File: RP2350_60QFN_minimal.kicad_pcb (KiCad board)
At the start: 2 copper layers, 52 x 51 mm, 43 parts, among them J1 USB_B_Micro, J2 Conn_02x18_Odd_Even, J3 Conn_02x18_Odd_Even, J4 SM03B-SRSS-TB, SW1 SW_Push, SW2 SW_Push, U1 RP2350_60QFN, U2 NCP1117-3.3_SOT223, U3 W25Q128JVS, Y1 ABM8-272-T3

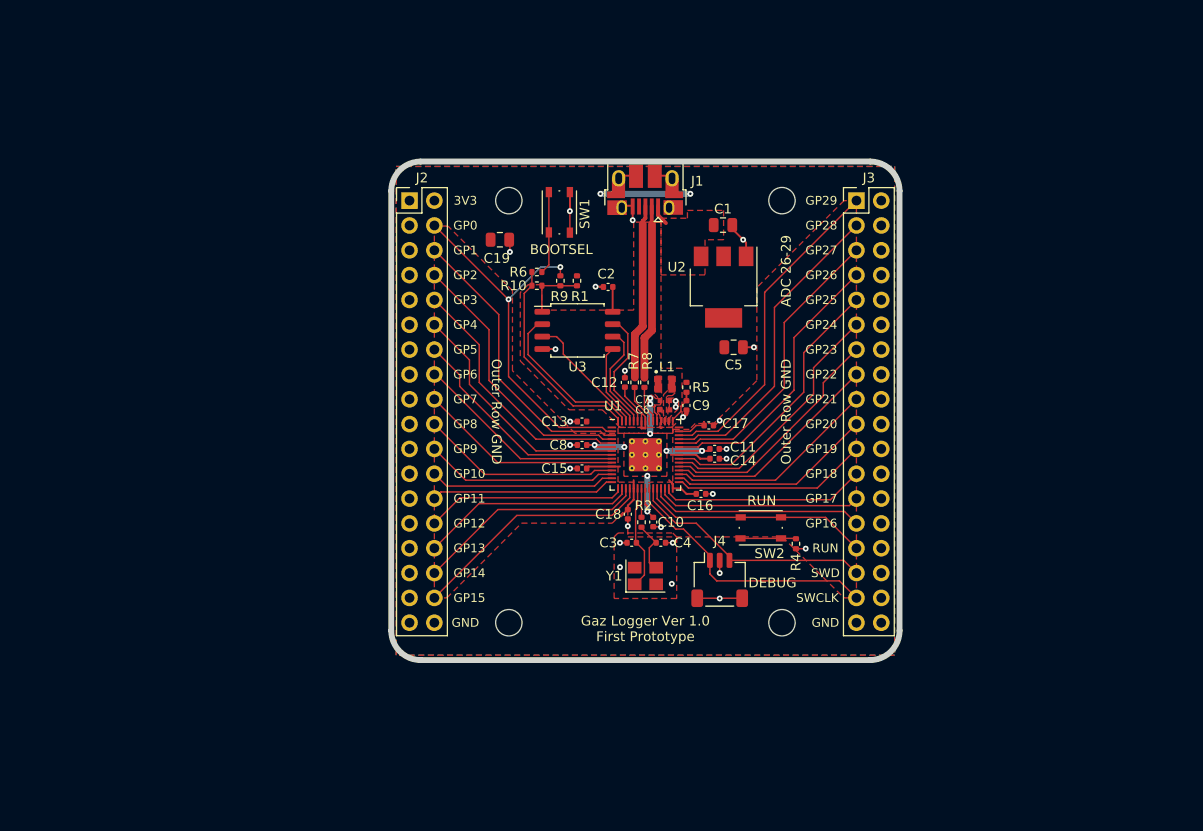
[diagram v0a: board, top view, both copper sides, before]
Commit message: improve design
Improve design, added multiplexer
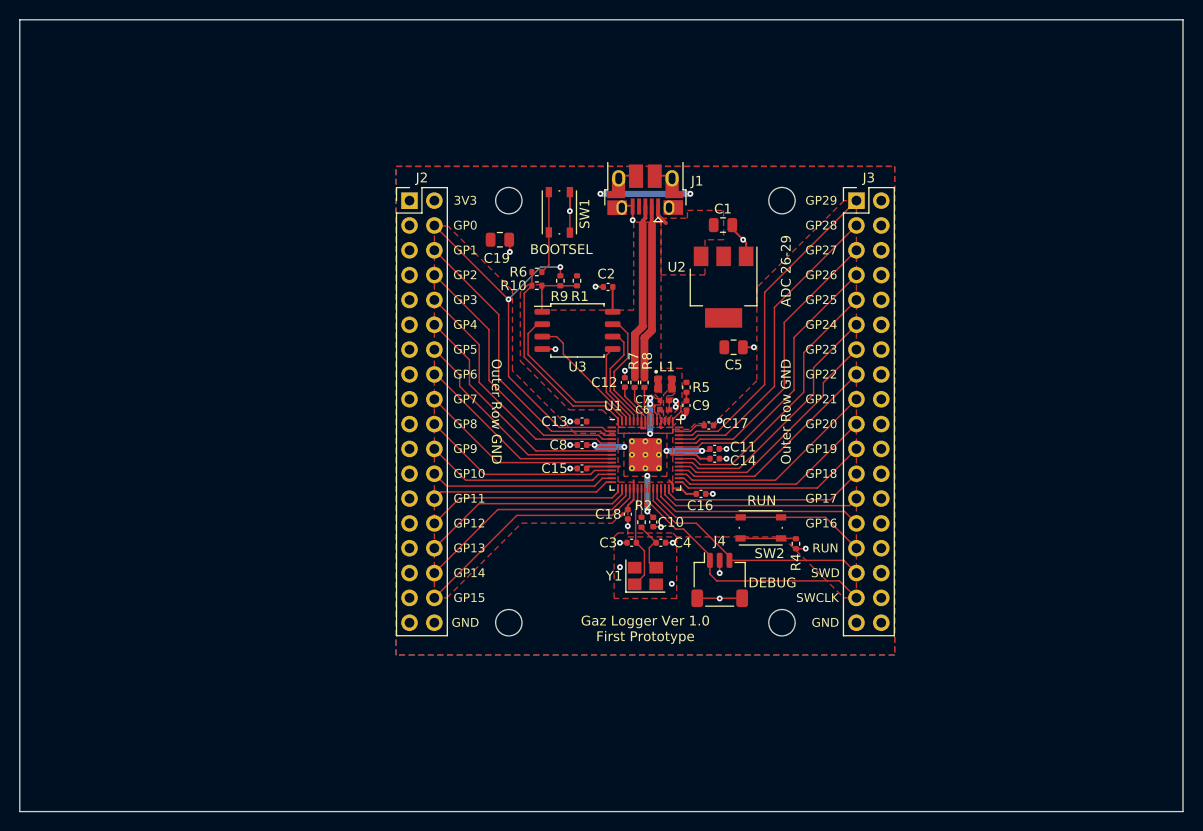
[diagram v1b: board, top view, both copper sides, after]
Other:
- board size 52 x 51 mm -> 119 x 81 mm
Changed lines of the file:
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@@
 		)
 	)
-	(gr_line
-		(start 123 121)
-		(end 77 121)
+	(gr_rect
+		(start 36 55.5)
+		(end 155 136.5)
 		(stroke
-			(width 0.6)
-			(type solid)
+			(width 0.05)
+			(type default)
 		)
+		(fill none)
 		(layer "Edge.Cuts")
 	)
-	(gr_line
-		(start 126 73)
-		(end 126 118)
-		(stroke
-			(width 0.6)
-			(type solid)
-		)
-		(layer "Edge.Cuts")
-	)
-	(gr_line
-		(start 77 70)
-		(end 123 70)
-		(stroke
-			(width 0.6)
-			(type solid)
-		)
-		(layer "Edge.Cuts")
-	)
-	(gr_line
-		(start 74 118)
-		(end 74 73)
-		(stroke
-			(width 0.6)
-			(type solid)
-		)
-		(layer "Edge.Cuts")
-	)
-	(gr_arc
-		(start 123 70)
-		(mid 125.12132 70.87868)
-		(end 126 73)
-		(stroke
-			(width 0.6)
-			(type solid)
-		)
-		(layer "Edge.Cuts")
-	)
-	(gr_arc
-		(start 74 73)
-		(mid 74.87868 70.87868)
-		(end 77 70)
-		(stroke
-			(width 0.6)
-			(type solid)
-		)
-		(layer "Edge.Cuts")
-	)
-	(gr_arc
-		(start 77 121)
-		(mid 74.87868 120.12132)
-		(end 74 118)
-		(stroke
-			(width 0.6)
-			(type solid)
-		)
-		(layer "Edge.Cuts")
-	)
-	(gr_arc
-		(start 126 118)
-		(mid 125.12132 120.12132)
-		(end 123 121)
-		(stroke
-			(width 0.6)
-			(type solid)
-		)
-		(layer "Edge.Cuts")
-	)

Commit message: added resistors matrics
added resistors matrics
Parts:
- removed C3, C4: 15p, Capacitor_SMD:C_0402_1005Metric
- removed R2: 1k, Resistor_SMD:R_0402_1005Metric
- removed Y1: ABM8-272-T3, Crystal:Crystal_SMD_3225-4Pin_3.2x2.5mm
- added C20: 15p, Capacitor_SMD:C_0402_1005Metric, F.Cu at (98.5, 109.0)
- added C21: 100nF, Capacitor_SMD:C_0402_1005Metric, F.Cu at (70.0, 76.0)
- added C22: 15p, Capacitor_SMD:C_0402_1005Metric, F.Cu at (101.5, 109.0)
- added C25: 1nF, Capacitor_SMD:C_0402_1005Metric, F.Cu at (64.0, 72.5)
- added C26: 100nF, Capacitor_SMD:C_0402_1005Metric, F.Cu at (100.5, 154.5)
- added GDT1: ~, Spark-2031-42T-SM-RPLF:TVS_2031-42T-SM-RPLF, F.Cu at (22.0, 170.0)
- added R(ACH)1: 1M, Resistor_SMD:R_0805_2012Metric_Pad1.20x1.40mm_HandSolder, F.Cu at (49.5, 67.5)
- added R11: 620k, Resistor_SMD:R_0805_2012Metric_Pad1.20x1.40mm_HandSolder, F.Cu at (23.5, 87.0)
- added R12: 390k, Resistor_SMD:R_0805_2012Metric_Pad1.20x1.40mm_HandSolder, F.Cu at (23.5, 89.5)
- added R13: 240k, Resistor_SMD:R_0805_2012Metric_Pad1.20x1.40mm_HandSolder, F.Cu at (23.5, 92.0)
- added R14: 160k, Resistor_SMD:R_0805_2012Metric_Pad1.20x1.40mm_HandSolder, F.Cu at (23.5, 94.5)
- added R15: 100k, Resistor_SMD:R_0805_2012Metric_Pad1.20x1.40mm_HandSolder, F.Cu at (23.5, 97.0)
- added R16: 62k, Resistor_SMD:R_0805_2012Metric_Pad1.20x1.40mm_HandSolder, F.Cu at (23.5, 99.5)
- added R17: 39k, Resistor_SMD:R_0805_2012Metric_Pad1.20x1.40mm_HandSolder, F.Cu at (23.5, 102.0)
- added R18: 24k, Resistor_SMD:R_0805_2012Metric_Pad1.20x1.40mm_HandSolder, F.Cu at (23.5, 104.5)
- added R19: 16k, Resistor_SMD:R_0805_2012Metric_Pad1.20x1.40mm_HandSolder, F.Cu at (23.5, 107.0)
- added R20: 10k, Resistor_SMD:R_0805_2012Metric_Pad1.20x1.40mm_HandSolder, F.Cu at (23.5, 109.5)
- added R21: 6.2k, Resistor_SMD:R_0805_2012Metric_Pad1.20x1.40mm_HandSolder, F.Cu at (23.5, 112.0)
- added R22: 3.9k, Resistor_SMD:R_0805_2012Metric_Pad1.20x1.40mm_HandSolder, F.Cu at (23.5, 114.5)
- added R23: 2.4k, Resistor_SMD:R_0805_2012Metric_Pad1.20x1.40mm_HandSolder, F.Cu at (23.5, 117.0)
- added R24: 1.6k, Resistor_SMD:R_0805_2012Metric_Pad1.20x1.40mm_HandSolder, F.Cu at (23.5, 119.5)
- added R25: 1k, Resistor_SMD:R_0805_2012Metric_Pad1.20x1.40mm_HandSolder, F.Cu at (23.5, 122.0)
- added R26: 1k, Resistor_SMD:R_0402_1005Metric, F.Cu at (99.5, 107.0)
- added R27: 10k, Resistor_SMD:R_0805_2012Metric_Pad1.20x1.40mm_HandSolder, F.Cu at (32.8, 69.5)
- added R28: 10k, Resistor_SMD:R_0805_2012Metric_Pad1.20x1.40mm_HandSolder, F.Cu at (32.8, 72.4)
- added R29: 10k, Resistor_SMD:R_0805_2012Metric_Pad1.20x1.40mm_HandSolder, F.Cu at (32.8, 75.3)
- added R3: 1M, Resistor_SMD:R_0805_2012Metric_Pad1.20x1.40mm_HandSolder, F.Cu at (23.5, 84.5)
- added U4: CD74HC4067SM96G4, CD74HC4067SM96G4:SOP65P780X200-24N, F.Cu at (64.0, 77.5)
- added U5: TLV9002IDGKR, TLV9002IDGKR:SOP65P490X110-8N, F.Cu at (23.0, 146.0)
- added U6: ADS1115IDGSR, ADS1115IDGSR:SOP50P490X110-10N, F.Cu at (41.5, 143.5)
- added U7: PCA9306DP1_125, PCA9306DP1_125:SOP65P400X110-8N, F.Cu at (53.0, 147.0)
- added Y2: ABM8-272-T3, Crystal:Crystal_SMD_3225-4Pin_3.2x2.5mm, F.Cu at (100.1, 112.3)
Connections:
- J2 pad 1: GND -> VBUS
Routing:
- net VBUS: track 2.11 -> 47.2 mm
- net GND: track 37.5 -> 68.6 mm, vias 27 -> 29
- net /GPIO0: track 39.0 -> 59.2 mm, vias 2 -> 4
- net /GPIO1: track 29.8 -> 49.2 mm, vias 0 -> 2
- net /GPIO3: track 26.5 -> 38.7 mm
- net /GPIO2: track 28.2 -> 39.6 mm
- net Net-(C4-Pad1): track 5.42 -> 0.00 mm
- net Net-(C22-Pad1): track 0.00 -> 5.42 mm
- net Net-(U4-COMMON_I/O): track 0.00 -> 3.64 mm
- net +3V3: track 37.6 -> 41.2 mm

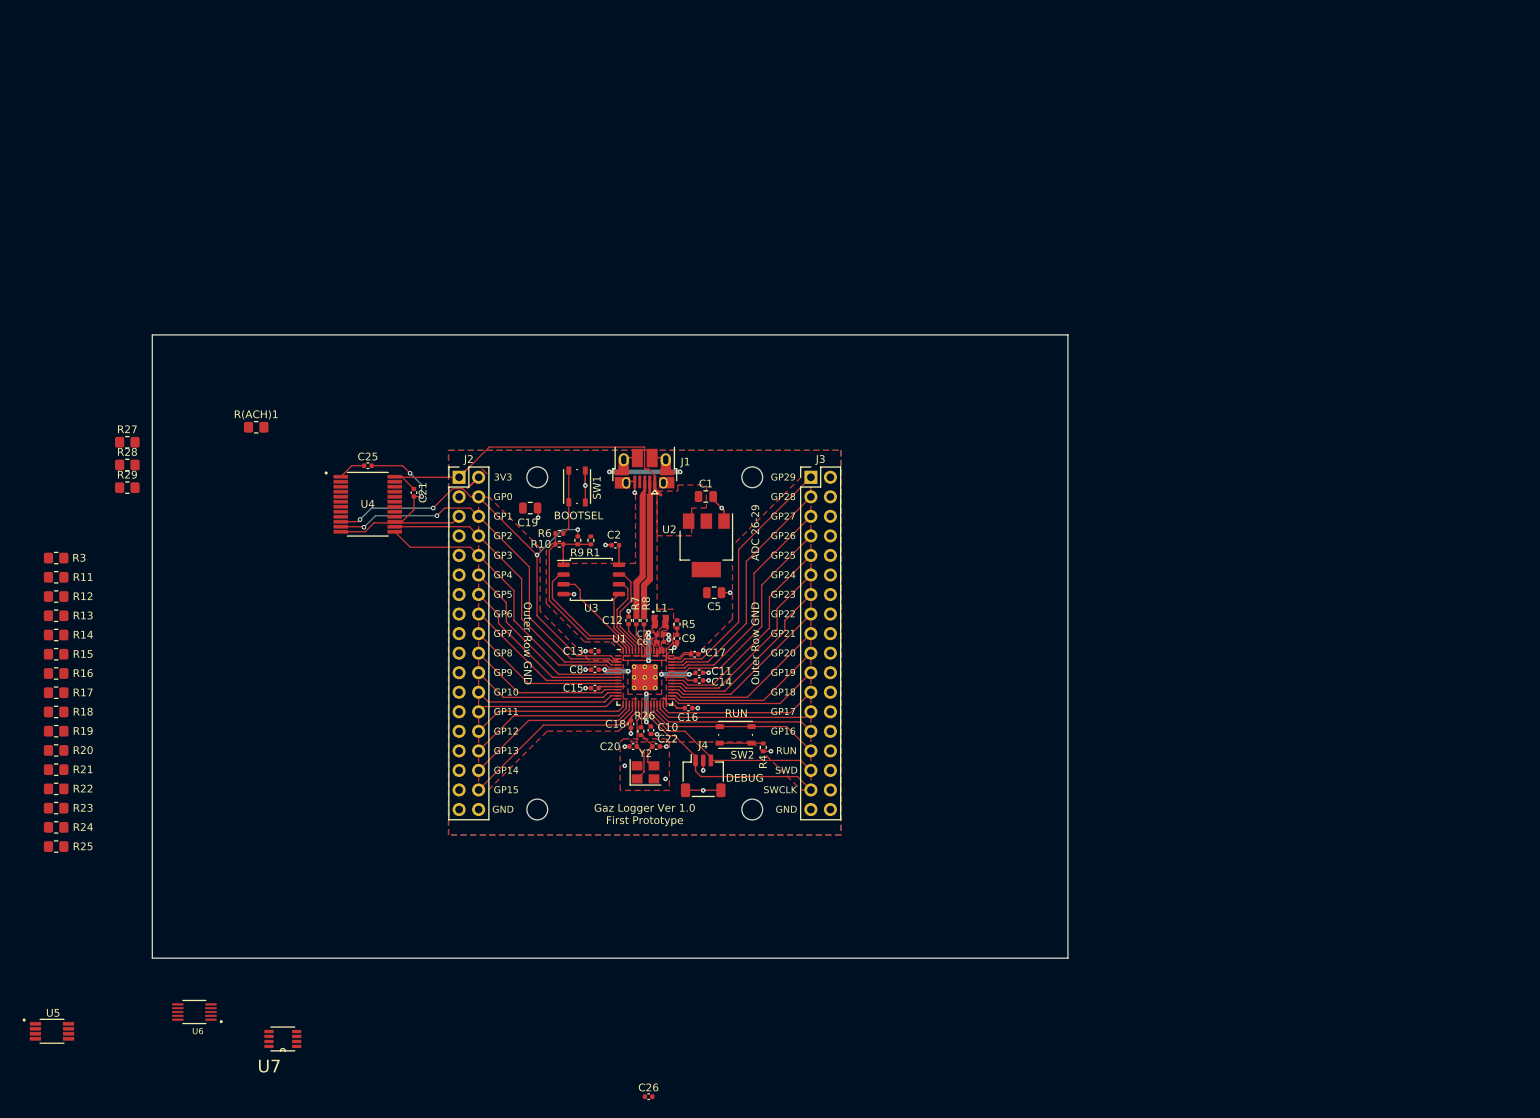
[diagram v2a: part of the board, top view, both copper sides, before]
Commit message: updare resistor matrix
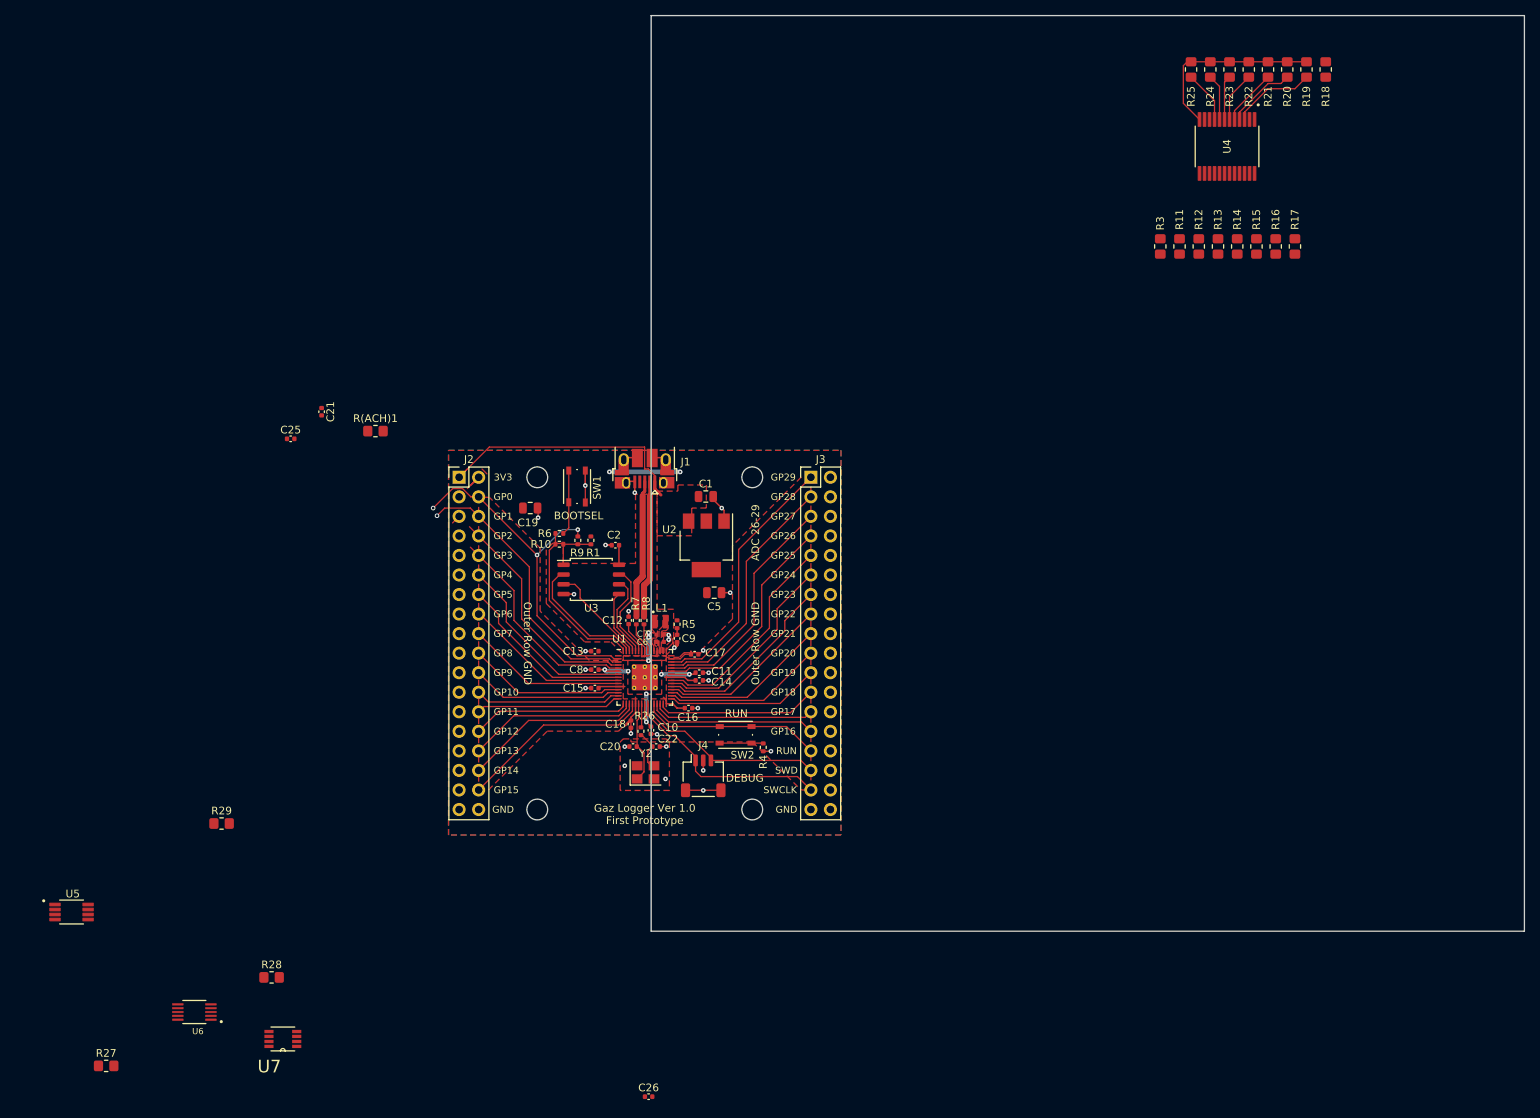
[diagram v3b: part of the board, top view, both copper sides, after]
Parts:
- moved R18 184.9 mm to (188.5, 21.0), turned to 90 degrees
- moved R19 183.9 mm to (186.0, 21.0), turned to 90 degrees
- moved R20 182.8 mm to (183.5, 21.0), turned to 90 degrees
- moved R21 181.9 mm to (181.0, 21.0), turned to 90 degrees
- moved R22 181.0 mm to (178.5, 21.0), turned to 90 degrees
- moved R23 180.2 mm to (176.0, 21.0), turned to 90 degrees
- moved R24 179.4 mm to (173.5, 21.0), turned to 90 degrees
- moved R25 178.8 mm to (171.0, 21.0), turned to 90 degrees
- moved R17 171.1 mm to (184.5, 44.0), turned to -90 degrees
- moved R16 167.9 mm to (182.0, 44.0), turned to -90 degrees
- moved R15 164.8 mm to (179.5, 44.0), turned to -90 degrees
- moved R14 161.6 mm to (177.0, 44.0), turned to -90 degrees
- moved R13 158.4 mm to (174.5, 44.0), turned to -90 degrees
- moved R12 155.3 mm to (172.0, 44.0), turned to -90 degrees
- moved R11 152.2 mm to (169.5, 44.0), turned to -90 degrees
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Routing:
- net /GPIO1: track 49.2 -> 36.1 mm, vias 2 -> 1
- net /GPIO0: track 59.2 -> 46.4 mm, vias 4 -> 3
- net VBUS: track 47.2 -> 35.6 mm
- net Net-(U4-I6): track 0.00 -> 10.9 mm
- net /GPIO3: track 38.7 -> 28.0 mm
- net /GPIO2: track 39.6 -> 29.8 mm
- net Net-(U4-I5): track 0.00 -> 9.03 mm
- net Net-(U4-I4): track 0.00 -> 7.30 mm
- net Net-(U4-I0): track 0.00 -> 6.76 mm
- net Net-(U4-I3): track 0.00 -> 6.54 mm
- net Net-(U4-I1): track 0.00 -> 6.00 mm
- net Net-(U4-I2): track 0.00 -> 5.77 mm
- net GND: track 68.6 -> 63.3 mm, vias 29 -> 27
- net Net-(U4-COMMON_I/O): track 3.64 -> 0.00 mm
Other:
- board size 119 x 81 mm -> 113.5 x 119 mm

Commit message: Update shematic, before connect to board
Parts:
- U5: value TLV9002IDGKR -> TLV
- moved GDT1 222.4 mm to (204.5, 43.0), turned to 180 degrees
- moved R27 203.8 mm to (205.5, 47.0)
- moved U5 185.9 mm to (192.0, 47.8)
- moved U6 180.3 mm to (191.8, 44.0), turned to 0 degrees
- moved U7 179.1 mm to (199.5, 44.0), turned to 90 degrees
- moved R28 171.3 mm to (197.5, 49.5), turned to -90 degrees
- moved R29 164.8 mm to (195.5, 52.0), turned to -90 degrees
- moved C5 151.1 mm to (257.4, 60.2)
- moved H2 151.1 mm to (262.3, 45.2)
- moved H3 151.1 mm to (262.3, 88.3)
- moved J3 151.1 mm to (269.9, 45.2)
- moved C1 151.1 mm to (256.3, 47.7)
- moved C10 151.1 mm to (249.1, 78.0)
- moved C11 151.1 mm to (255.4, 70.6)
- moved C12 151.1 mm to (246.2, 63.8)
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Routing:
- net GND: track 63.3 -> 128.9 mm
- net VBUS: track 35.6 -> 56.0 mm
- net Net-(U4-COMMON_I/O): track 0.00 -> 13.3 mm
- net Net-(U4-I7): track 0.00 -> 12.7 mm
- net Net-(U4-I8): track 0.00 -> 12.7 mm
- net Net-(U6-ALERT/RDY): track 0.00 -> 11.3 mm
- net Net-(U4-I9): track 0.00 -> 10.9 mm
- net Net-(U4-I10): track 0.00 -> 9.03 mm
- net Net-(U4-I11): track 0.00 -> 7.29 mm
- net Net-(U4-I15): track 0.00 -> 6.75 mm
- net Net-(U4-I12): track 0.00 -> 6.53 mm
- net Net-(U6-VDD): track 0.00 -> 6.38 mm
- net Net-(U4-I14): track 0.00 -> 5.99 mm
- net Net-(U4-I13): track 0.00 -> 5.76 mm
- net +3V3: track 41.2 -> 46.1 mm
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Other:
- board size 113.5 x 119 mm -> 270 x 119 mm

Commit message: finish first design
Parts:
- added R30: 4.7k, Resistor_SMD:R_0805_2012Metric_Pad1.20x1.40mm_HandSolder, F.Cu at (154.5, 66.5)
- added R31: 4.7k, Resistor_SMD:R_0805_2012Metric_Pad1.20x1.40mm_HandSolder, F.Cu at (156.5, 66.5)
- U5: value TLV -> TLV9002IDGKR
- U7: value PCA9306DP1_125 -> PCA9306
- moved GDT1 90.5 mm to (119.9, 75.1), turned to 90 degrees
- moved R27 86.2 mm to (126.4, 81.1), turned to 180 degrees
- moved U7 76.9 mm to (126.5, 68.1), turned to 180 degrees
- moved U6 72.6 mm to (126.5, 75.8), turned to 90 degrees
- moved R17 72.4 mm to (131.5, 65.6), turned to 90 degrees
- moved R16 69.4 mm to (134.0, 65.6), turned to 90 degrees
- moved R28 68.6 mm to (132.0, 70.1), turned to 0 degrees
- moved U5 67.6 mm to (130.4, 75.6), turned to 90 degrees
- moved R15 66.5 mm to (136.5, 65.6), turned to 90 degrees
- moved C18 65.1 mm to (185.9, 100.9)
- moved C20 65.1 mm to (186.2, 103.8)
- moved C22 65.1 mm to (189.2, 103.8)
- moved C5 65.1 mm to (196.7, 83.8)
- moved C9 65.1 mm to (191.9, 89.7)
- moved H2 65.1 mm to (201.7, 68.8)
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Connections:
- J2 pad 1: VBUS -> GND
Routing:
- net /GPIO4: track 25.0 -> 81.3 mm, vias 0 -> 2
- net +3V3: track 46.1 -> 101.6 mm, vias 2 -> 4
- net /GPIO5: track 23.3 -> 77.6 mm, vias 0 -> 2
- net VBUS: track 56.0 -> 93.2 mm, vias 0 -> 3
- net /GPIO2: track 29.8 -> 51.9 mm
- net /GPIO3: track 28.0 -> 48.2 mm
- net GND: track 128.9 -> 148.0 mm
- net /GPIO0: track 46.4 -> 64.7 mm, vias 3 -> 4
- net /GPIO1: track 36.1 -> 53.9 mm, vias 1 -> 2
- net /I2C_SDA_5V: track 0.00 -> 8.54 mm
- net /I2C_SCL_5V: track 0.00 -> 7.18 mm
- net Net-(U6-ADDR): track 4.73 -> 9.30 mm
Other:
- board size 270 x 119 mm -> 105.5 x 65.5 mm
